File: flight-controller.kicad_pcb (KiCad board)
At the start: 4 copper layers, 29 x 43 mm, 50 parts, among them J1 USB_C_Receptacle_USB2.0_16P, J2 Conn_Coaxial, J4 TC2030, SW1 SW_Push, U1 MIC5365-3.3YD5, U2 USBLC6-2SC6, U3 DLF162500LT-5028A1, U4 STM32WB55CEUx, U5 MPU-6050, X1 32kHz768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

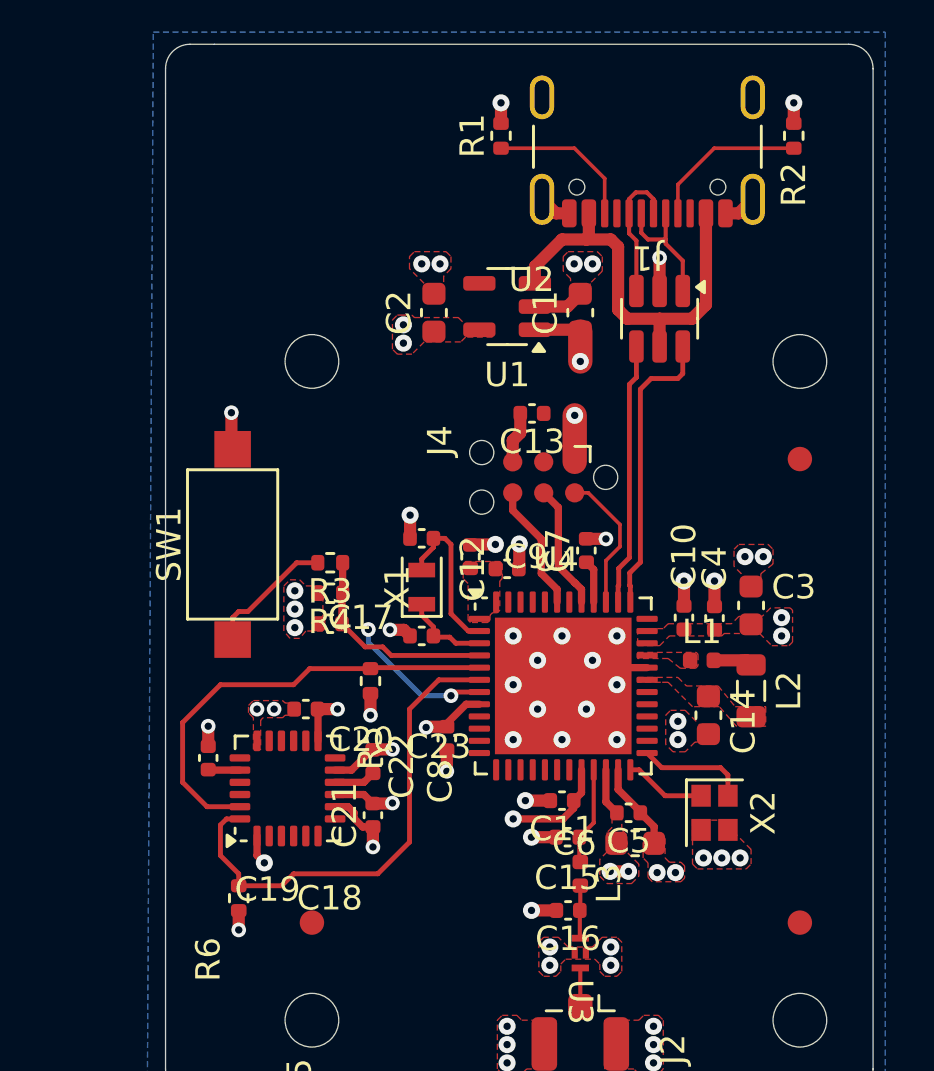
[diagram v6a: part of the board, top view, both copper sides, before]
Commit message: BOM done, footprints & layout updated.
Layout for both crystal oscillators revised.
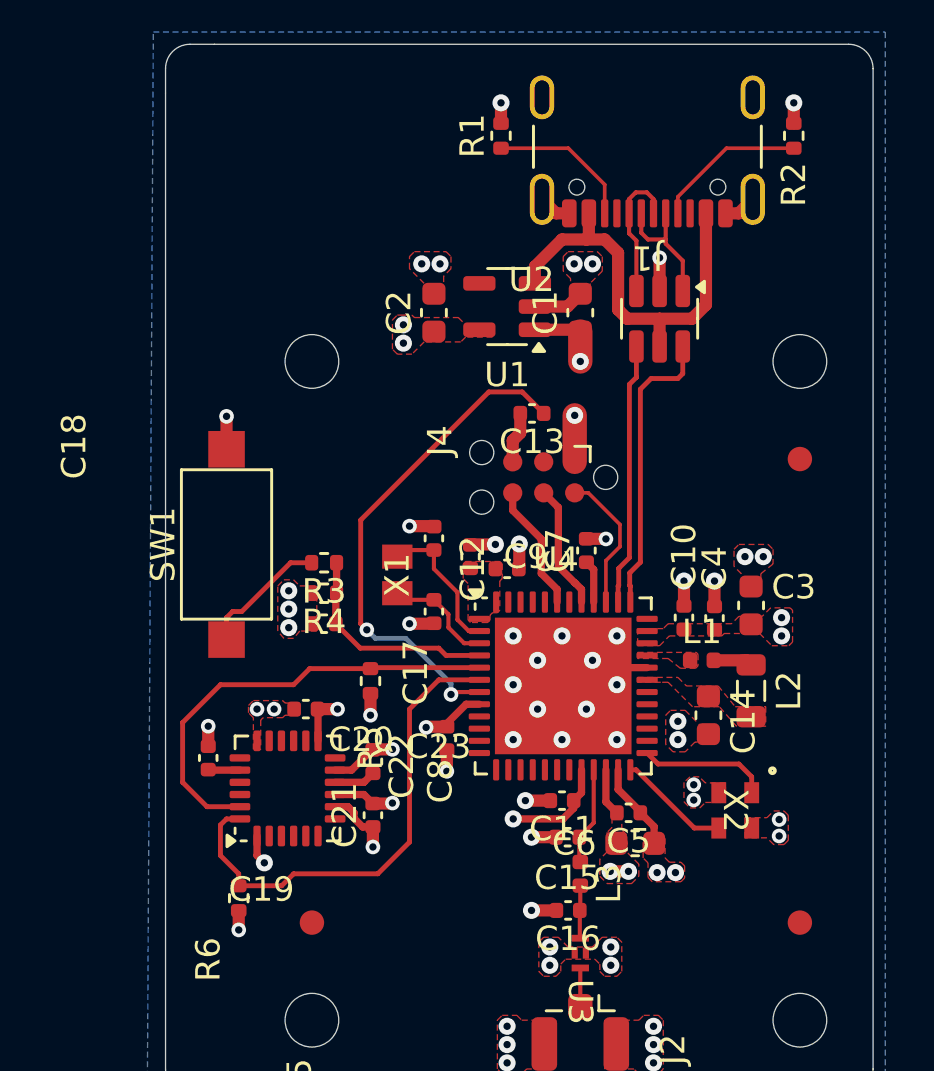
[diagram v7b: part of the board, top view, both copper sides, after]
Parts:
- X1: footprint Crystal:Crystal_SMD_2012-2Pin_2.0x1.2mm -> Library:XTAL_NX2012SA_NDK
- X2: value 32MHz -> NX2016SA-32M; footprint Crystal:Crystal_SMD_2016-4Pin_2.0x1.6mm -> Library:NX2016SA_NDK
- moved C17 1.12 mm to (97.0, 97.2), turned to -90 degrees
- moved X1 1.12 mm to (95.5, 95.8)
- moved X2 0.86 mm to (109.3, 105.4)
- moved C18 0.50 mm to (97.0, 94.2), turned to 90 degrees
- moved C19 0.25 mm to (92.5, 97.8)
- moved R3 0.25 mm to (92.5, 95.2)
- moved R4 0.25 mm to (92.5, 96.5)
- moved SW1 0.25 mm to (88.5, 94.5)
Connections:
- X2 pad 1: /HSE_OUT -> /HSE_IN
- X2 pad 3: GND -> /HSE_OUT
- X2 pad 4: /HSE_IN -> GND
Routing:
- net /SWD_NRST: track 6.06 -> 20.7 mm
- net /HSE_OUT: track 3.34 -> 4.61 mm
- net /LSE_OUT: track 3.51 -> 4.53 mm
- net /LSE_IN: track 6.78 -> 5.96 mm
- net /HSE_IN: track 4.54 -> 5.34 mm
- net GND: track 37.3 -> 37.4 mm, vias 58 -> 59

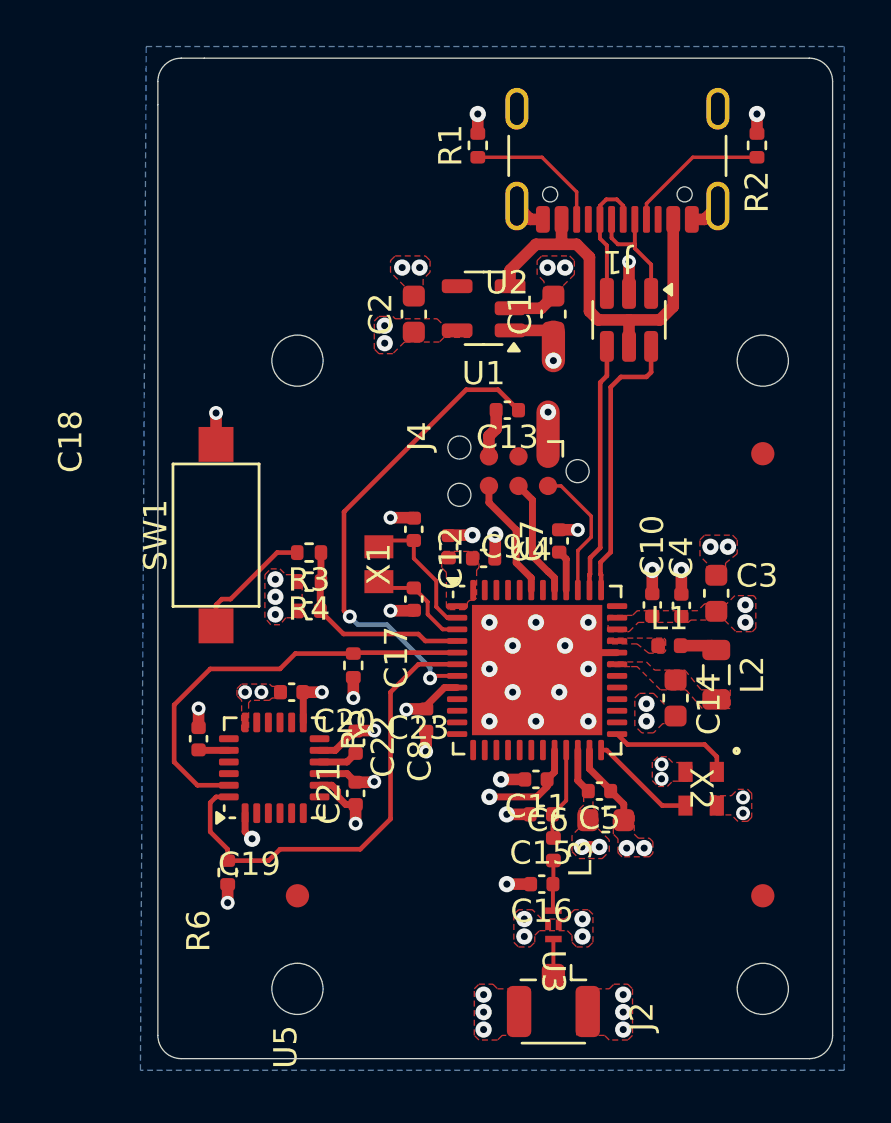
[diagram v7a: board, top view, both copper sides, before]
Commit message: almost no DRC errors
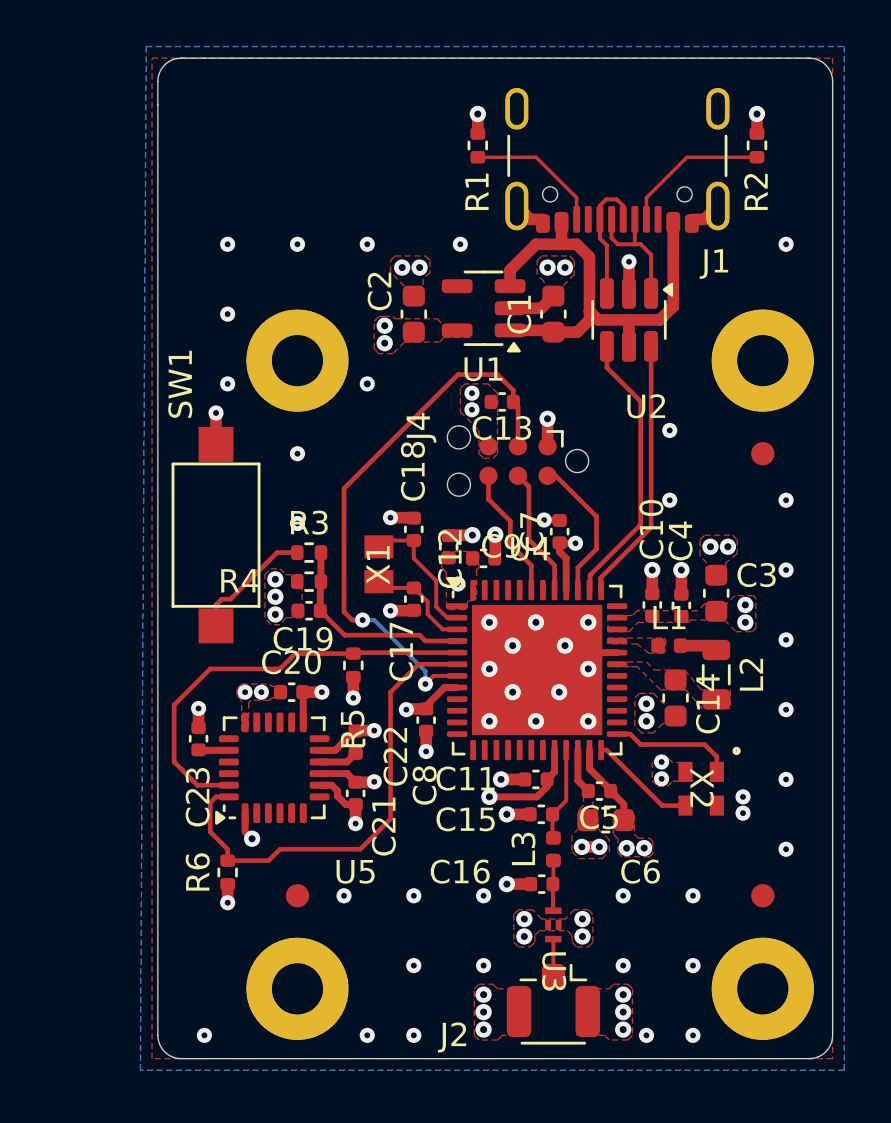
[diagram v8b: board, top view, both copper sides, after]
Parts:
- H1, H2, H3, H4: footprint MountingHole:MountingHole_2.2mm_M2 -> MountingHole:MountingHole_2.2mm_M2_Pad
- moved J4 0.44 mm to (101.5, 91.3)
- moved C13 0.42 mm to (100.8, 88.8)
- moved C7 0.40 mm to (103.3, 94.3)
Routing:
- net /SWD_NRST: track 20.7 -> 24.0 mm
- net GND: track 37.4 -> 35.1 mm, vias 59 -> 93
- net /USB_D+: track 16.5 -> 17.7 mm
- net +5V: track 20.2 -> 21.1 mm, vias 1 -> 0
- net /SWD_DIO: track 5.81 -> 6.33 mm
- net +3V3: track 22.6 -> 22.9 mm, vias 14 -> 16
